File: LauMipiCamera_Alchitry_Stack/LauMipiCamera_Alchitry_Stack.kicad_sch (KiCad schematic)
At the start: 10 parts, among them J1 DF40C-50DP, J2 DF40C-80DP, J3 DF40C-80DP, SW1 SW_DIP_x4

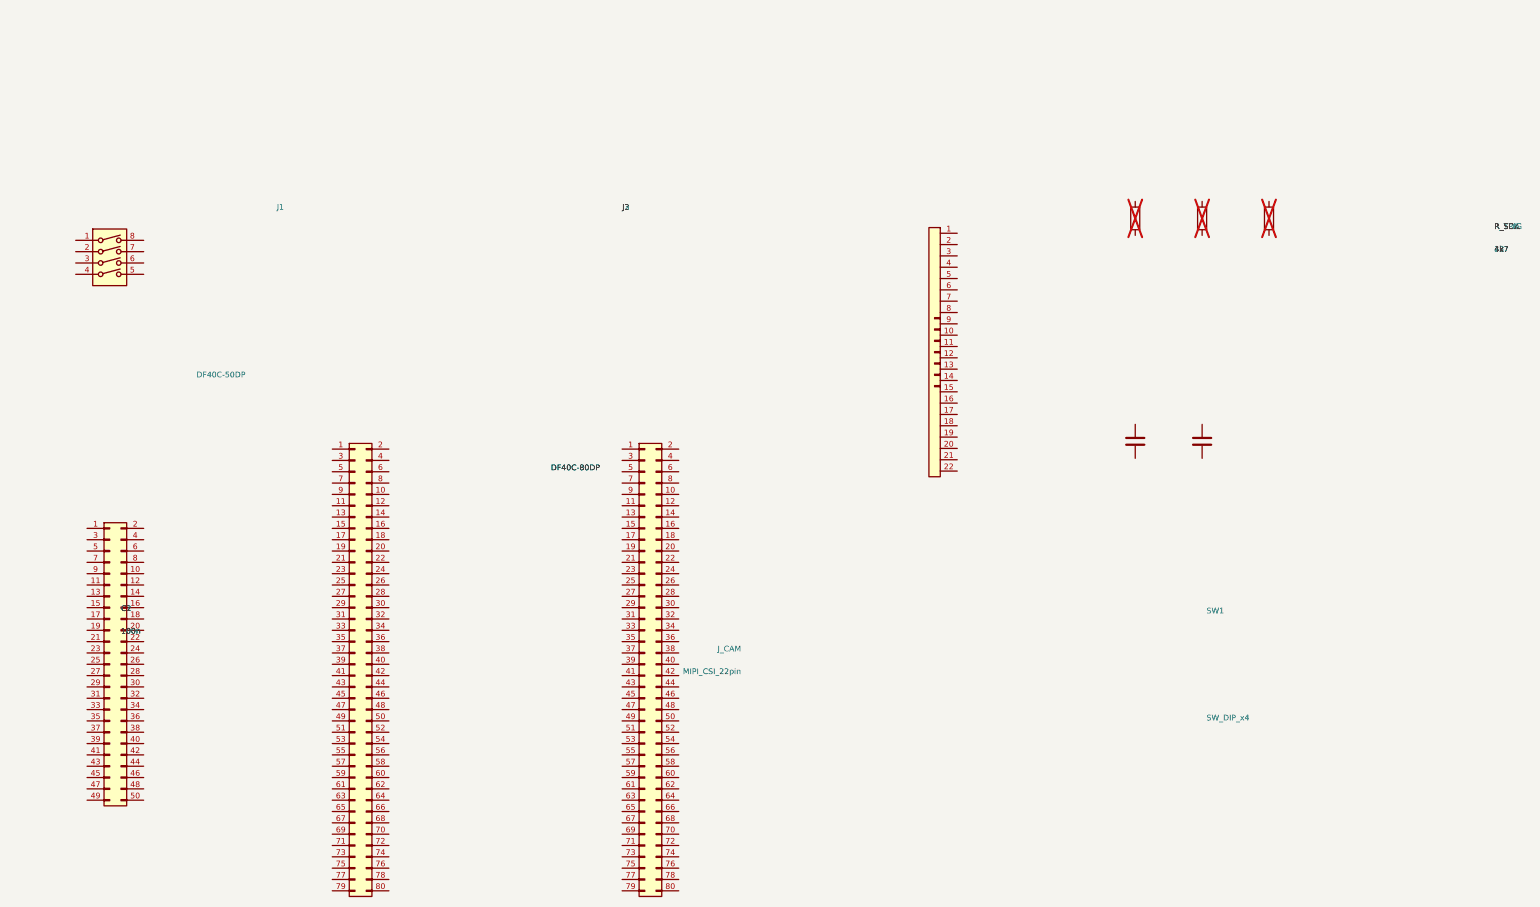
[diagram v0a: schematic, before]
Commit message: hw(mipi): wire the schematic -- 23 nets, XAPP894 front end, explicit no-connects
The scaffold had 10 symbols and zero connectivity (no wires, no labels, no
nets). Net it out per SCHEMATIC.md, add the 9 XAPP894 front-end resistors, and
snap every pin endpoint onto the 1.27 mm grid.

Nets (verified with kicad-cli 10.0.3 `sch export netlist`): 23 real nets,
0 single-node nets, all 22 signal nets match the spec.
  * 3 HS pairs: camera -> J3, with R_T (150R) across each pair and R_LP*
    (100R) tapping each line to its HSUL_12 LP input
  * CAM_TRIG through R_TRIG (33R series) to the camera; CAM_STROBE direct
  * I2C pulled to +3V3 (camera abs max on those pins is 3.8 V)
  * J1 +3V3 on pins 1/3/5/9/11 (five contacts for ~260 mA); J2's 28 GND pins
    bonded for the HS return path; J3 GND on all 28 mod-6 pins

Decisions made while wiring, all recorded in SCHEMATIC.md:
  * Config switches wired SPST-to-GND (uniform, internal PULLUP) -- the placed
    footprint is an SPST slide DIP with no second throw, so the old SPDT
    "+3V3/GND" text was unbuildable. This also removes the rev-1 asymmetry
    where HvsV alone was tied high and needed inverted logic.
  * J1 pins 7/13 left NC: they are odd-1..13 (+3V3 by ROADMAP) *and* mod-6
    (GND by the 80-pin rule). Ambiguous, so not guessed.
  * CAM_STROBE lands on B18 (next free non-GND pin); its Pt V2 ball is NOT yet
    package-verified.

Also: fixed 4 dead footprint links (schematic pointed at Connector_Hirose and a
9.78x9.09 DIP that do not exist; the PCB carries the real ones), cleared the
scaffold's dnp=yes on R_SCL/R_SDA/R_TRIG, and made C2 a 10u bulk cap.

ERC: 157 violations -> 1 (a cached-symbol mismatch on Conn_01x22; refresh from
library in the GUI). The 133 pin_not_connected errors are now explicit
no_connect flags, and the 19 off-grid endpoints are gone.

Not yet done: update the PCB from this schematic (adds the 9 resistors, moves
R_SCL/R_SDA/R_TRIG from 1206 to 0402) and place the front end at J3 per SS3.4.

Co-Auth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
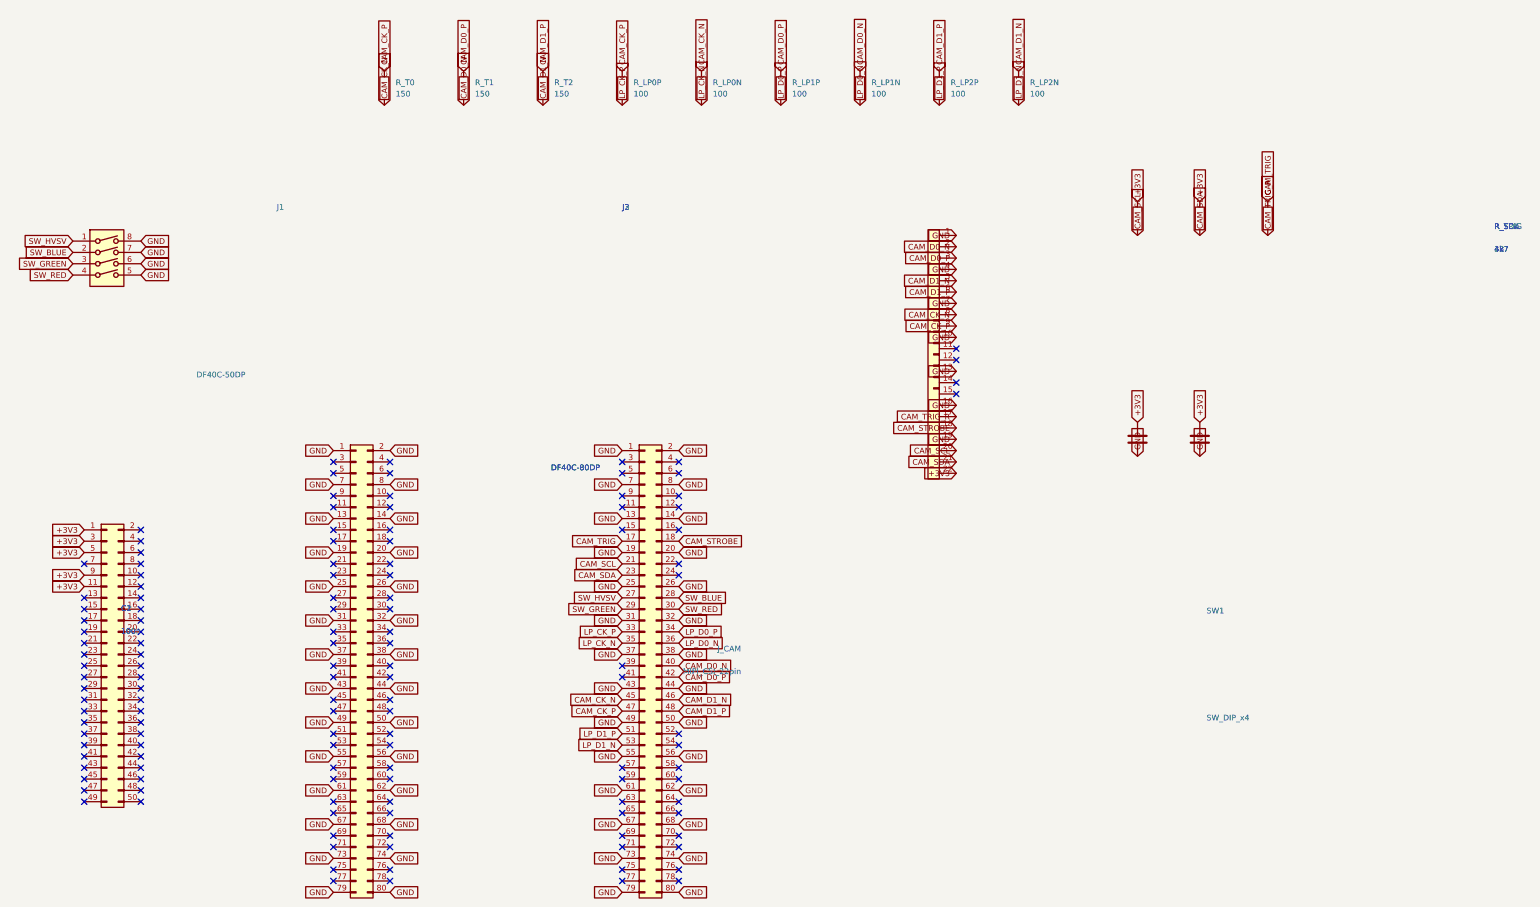
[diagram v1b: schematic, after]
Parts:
- added R_LP0N, R_LP0P, R_LP1N, R_LP1P, R_LP2N, R_LP2P: 100, Resistor_SMD:R_0402_1005Metric, symbol Device:R
- added R_T0, R_T1, R_T2: 150, Resistor_SMD:R_0402_1005Metric, symbol Device:R
- C1: footprint Capacitor_SMD:C_0402_1005Metric -> Capacitor_SMD:C_0805_2012Metric
- C2: value 100n -> 10u; footprint Capacitor_SMD:C_0402_1005Metric -> Capacitor_SMD:C_0805_2012Metric
- J1: footprint Connector_Hirose:Hirose_DF40C-50DP-0.4V_2x25_P0.40mm_Vertical -> Connector_Hirose_DF40:Hirose_DF40C-50DP-0.4V_2x25-1MP_P0.4mm
- J2, J3: footprint Connector_Hirose:Hirose_DF40C-80DP-0.4V_2x40_P0.40mm_Vertical -> Connector_Hirose_DF40:Hirose_DF40C-80DP-0.4V_2x40-1MP_P0.4mm
- R_SCL, R_SDA, R_TRIG: now fitted
- SW1: footprint Button_Switch_SMD:SW_DIP_SPSTx04_Slide_9.78x9.09mm_W7.62mm_P2.54mm -> Button_Switch_SMD:SW_DIP_SPSTx04_Slide_6.7x11.72mm_W8.61mm_P2.54mm_LowProfile
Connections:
- net GND: now reaches J3.1 (Pin_1)
- net GND: now also C1.2, C2.2, J2.1 (Pin_1), J2.13 (Pin_13), J2.14 (Pin_14), J2.19 (Pin_19), J2.2 (Pin_2), J2.20 (Pin_20), J2.25 (Pin_25), J2.26 (Pin_26), J2.31 (Pin_31), J2.32 (Pin_32), J2.37 (Pin_37), J2.38 (Pin_38), J2.43 (Pin_43), J2.44 (Pin_44), J2.49 (Pin_49), J2.50 (Pin_50), J2.55 (Pin_55), J2.56 (Pin_56), J2.61 (Pin_61), J2.62 (Pin_62), J2.67 (Pin_67), J2.68 (Pin_68), J2.7 (Pin_7), J2.73 (Pin_73), J2.74 (Pin_74), J2.79 (Pin_79), J2.8 (Pin_8), J2.80 (Pin_80), J3.13 (Pin_13), J3.14 (Pin_14), J3.19 (Pin_19), J3.2 (Pin_2), J3.20 (Pin_20), J3.25 (Pin_25), J3.26 (Pin_26), J3.31 (Pin_31), J3.32 (Pin_32), J3.37 (Pin_37), J3.38 (Pin_38), J3.43 (Pin_43), J3.44 (Pin_44), J3.49 (Pin_49), J3.50 (Pin_50), J3.55 (Pin_55), J3.56 (Pin_56), J3.61 (Pin_61), J3.62 (Pin_62), J3.67 (Pin_67), J3.68 (Pin_68), J3.7 (Pin_7), J3.73 (Pin_73), J3.74 (Pin_74), J3.79 (Pin_79), J3.8 (Pin_8), J3.80 (Pin_80), J_CAM.1 (Pin_1), J_CAM.10 (Pin_10), J_CAM.13 (Pin_13), J_CAM.16 (Pin_16), J_CAM.19 (Pin_19), J_CAM.4 (Pin_4), J_CAM.7 (Pin_7), SW1.5, SW1.6, SW1.7, SW1.8
- net CAM_TRIG: now reaches J3.17 (Pin_17)
- net CAM_TRIG: now also R_TRIG.1
- net CAM_STROBE: now reaches J3.18 (Pin_18)
- net CAM_STROBE: now also J_CAM.18 (Pin_18)
- net CAM_SCL: now reaches J3.21 (Pin_21)
- net CAM_SCL: now also J_CAM.20 (Pin_20), R_SCL.2
- net CAM_SDA: now reaches J3.23 (Pin_23)
- net CAM_SDA: now also J_CAM.21 (Pin_21), R_SDA.2
- net SW_HVSV: now reaches J3.27 (Pin_27)
- net SW_HVSV: now also SW1.1
- net SW_BLUE: now reaches J3.28 (Pin_28)
- net SW_BLUE: now also SW1.2
- net SW_GREEN: now reaches J3.29 (Pin_29)
- net SW_GREEN: now also SW1.3
- net SW_RED: now reaches J3.30 (Pin_30)
- net SW_RED: now also SW1.4
- net LP_CK_P: now reaches J3.33 (Pin_33)
- net LP_CK_P: now also R_LP0P.2
- net LP_D0_P: now reaches J3.34 (Pin_34)
- net LP_D0_P: now also R_LP1P.2
- net LP_CK_N: now reaches J3.35 (Pin_35)
- net LP_CK_N: now also R_LP0N.2
- net LP_D0_N: now reaches J3.36 (Pin_36)
- net LP_D0_N: now also R_LP1N.2
- net CAM_D0_N: now reaches J3.40 (Pin_40)
- net CAM_D0_N: now also J_CAM.2 (Pin_2), R_LP1N.1, R_T1.2
- net CAM_D0_P: now reaches J3.42 (Pin_42)
- net CAM_D0_P: now also J_CAM.3 (Pin_3), R_LP1P.1, R_T1.1
- net CAM_CK_N: now reaches J3.45 (Pin_45)
- net CAM_CK_N: now also J_CAM.8 (Pin_8), R_LP0N.1, R_T0.2
- net CAM_D1_N: now reaches J3.46 (Pin_46)
- net CAM_D1_N: now also J_CAM.5 (Pin_5), R_LP2N.1, R_T2.2
- net CAM_CK_P: now reaches J3.47 (Pin_47)
- net CAM_CK_P: now also J_CAM.9 (Pin_9), R_LP0P.1, R_T0.1
- net CAM_D1_P: now reaches J3.48 (Pin_48)
- net CAM_D1_P: now also J_CAM.6 (Pin_6), R_LP2P.1, R_T2.1
- net LP_D1_P: now reaches J3.51 (Pin_51)
- net LP_D1_P: now also R_LP2P.2
- net LP_D1_N: now reaches J3.53 (Pin_53)
- net LP_D1_N: now also R_LP2N.2
- net +3V3: now reaches J1.1 (Pin_1)
- net +3V3: now also C1.1, C2.1, J1.11 (Pin_11), J1.3 (Pin_3), J1.5 (Pin_5), J1.9 (Pin_9), J_CAM.22 (Pin_22), R_SCL.1, R_SDA.1
- net CAM_TRIG_R: now reaches J_CAM.17 (Pin_17)
- net CAM_TRIG_R: now also R_TRIG.2
- no-connect marks 0 -> 133
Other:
- moved on the sheet: C1, C2, J1, J_CAM, SW1
